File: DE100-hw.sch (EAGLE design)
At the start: 50 parts, among them IC3 74HC14D, IC4 74HC14D, U1 TLP521-4(GB), U2 TLP521-4(GB), X1 22-23-2041, X2 22-23-2031, X3 22-23-2101

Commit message: change route
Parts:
- removed H3: MOUNT-PAD-SQUARE3.0, holes:MOUNT-PAD-SQUARE3.0
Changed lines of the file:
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@@
 <part name="H1" library="holes" library_urn="urn:adsk.eagle:library:237" deviceset="MOUNT-PAD-SQUARE" device="3.0" package3d_urn="urn:adsk.eagle:package:14290/1"/>
 <part name="H2" library="holes" library_urn="urn:adsk.eagle:library:237" deviceset="MOUNT-PAD-SQUARE" device="3.0" package3d_urn="urn:adsk.eagle:package:14290/1"/>
-<part name="H3" library="holes" library_urn="urn:adsk.eagle:library:237" deviceset="MOUNT-PAD-SQUARE" device="3.0" package3d_urn="urn:adsk.eagle:package:14290/1"/>
 </parts>
 <sheets>
@@
 <attribute name="VALUE" x="165.354" y="2.6162" size="1.778" layer="96"/>
 </instance>
-<instance part="H3" gate="G$1" x="154.94" y="5.08" smashed="yes">
-<attribute name="NAME" x="157.734" y="5.6642" size="1.778" layer="95"/>
-<attribute name="VALUE" x="157.734" y="2.6162" size="1.778" layer="96"/>
-</instance>
 </instances>

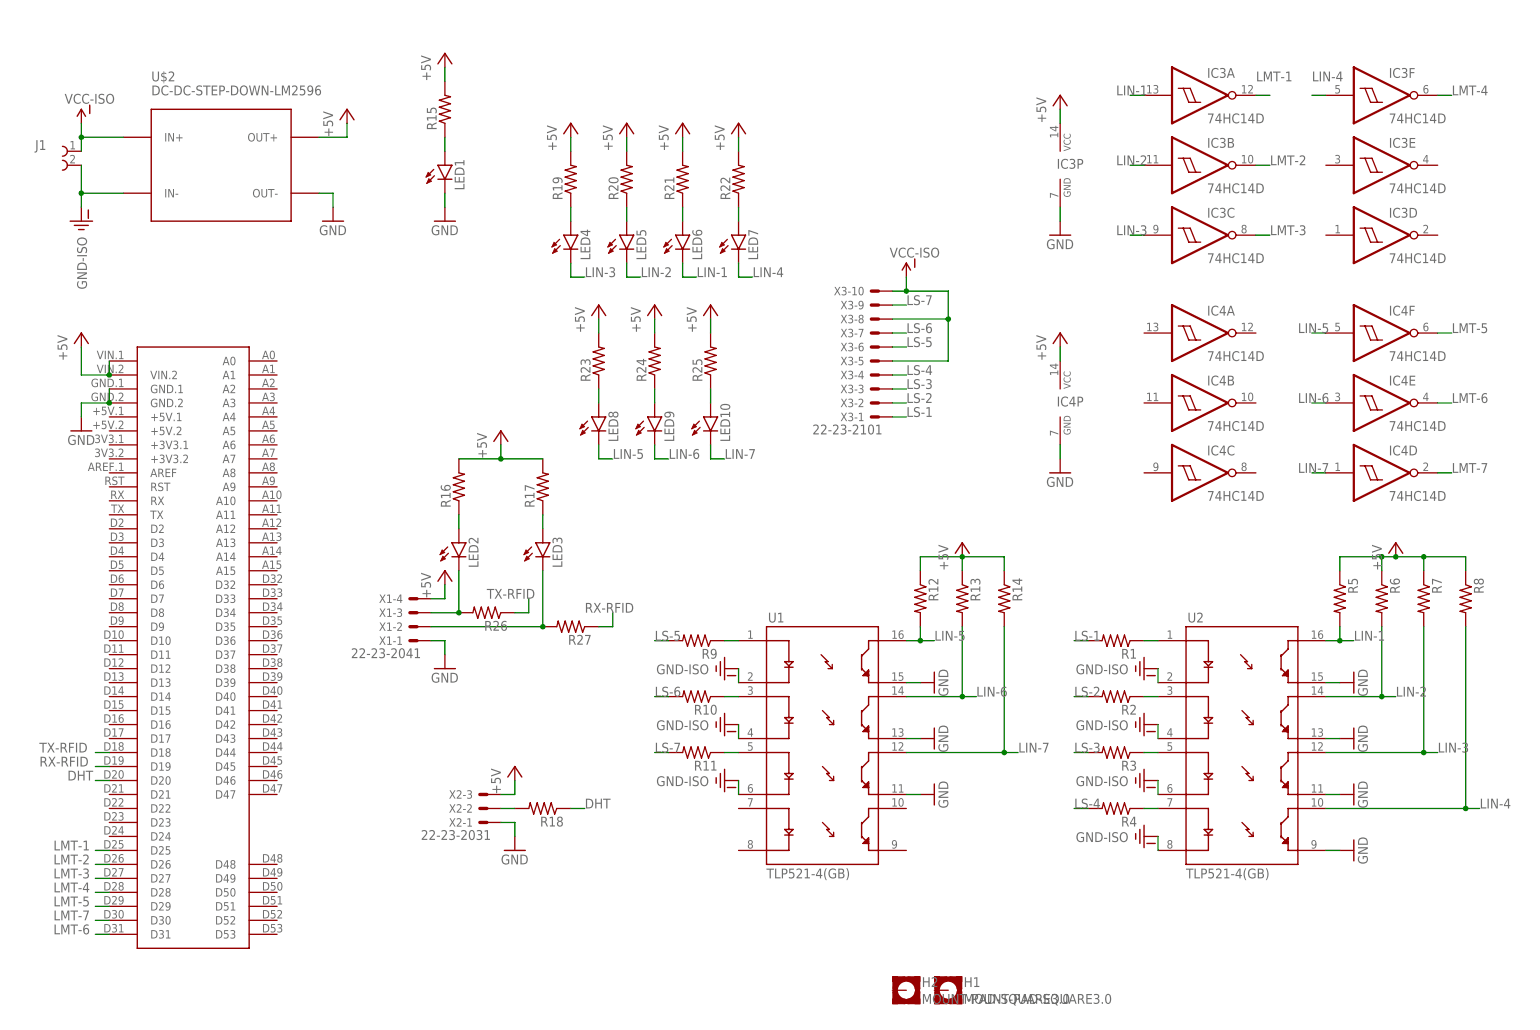
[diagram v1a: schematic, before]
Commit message: add additional name and gerber file
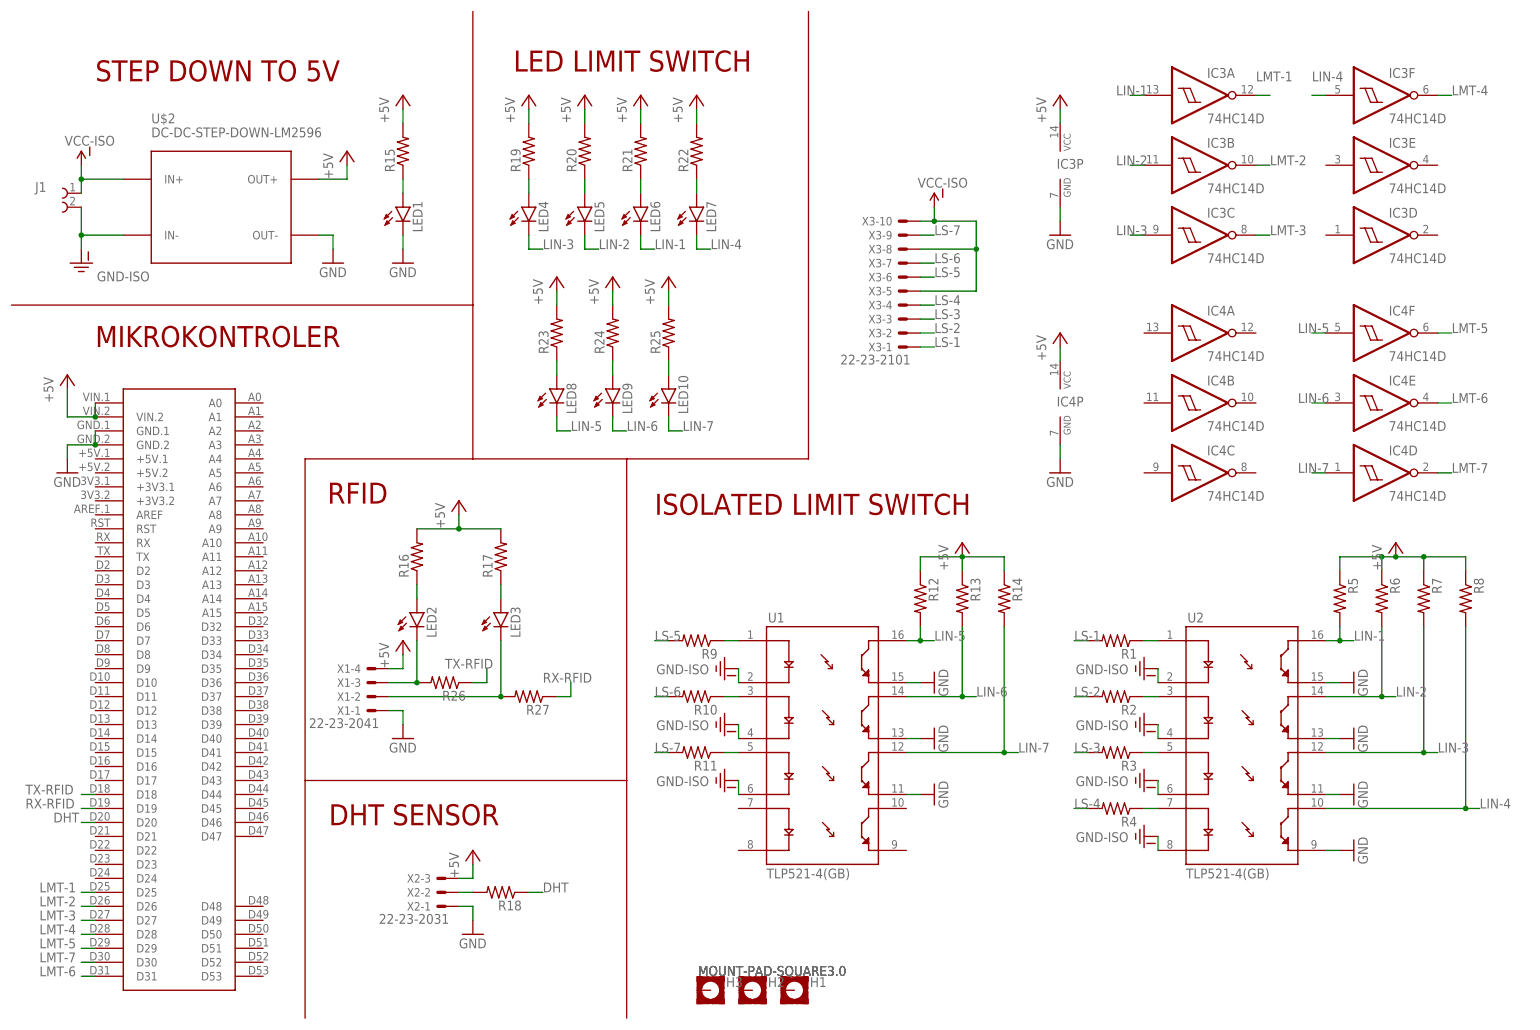
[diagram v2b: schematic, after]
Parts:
- added H3: MOUNT-PAD-SQUARE3.0, holes:MOUNT-PAD-SQUARE3.0
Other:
- note added: "DHT SENSOR"
- note added: "ISOLATED LIMIT SWITCH"
- note added: "LED LIMIT SWITCH"
- note added: "MIKROKONTROLER"
- note added: "RFID"
- note added: "STEP DOWN TO 5V"
- moved on the sheet: H1, H2, J1, LED1, LED10, LED2, LED3, LED4, LED5, LED6, LED7, LED8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

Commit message: add hole
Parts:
- added H4: MOUNT-PAD-SQUARE3.0, holes:MOUNT-PAD-SQUARE3.0
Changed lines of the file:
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@@
 <part name="H2" library="holes" library_urn="urn:adsk.eagle:library:237" deviceset="MOUNT-PAD-SQUARE" device="3.0" package3d_urn="urn:adsk.eagle:package:14290/1"/>
 <part name="H3" library="holes" library_urn="urn:adsk.eagle:library:237" deviceset="MOUNT-PAD-SQUARE" device="3.0" package3d_urn="urn:adsk.eagle:package:14290/1"/>
+<part name="H4" library="holes" library_urn="urn:adsk.eagle:library:237" deviceset="MOUNT-PAD-SQUARE" device="3.0" package3d_urn="urn:adsk.eagle:package:14290/1"/>
 </parts>
 <sheets>
@@
 <attribute name="VALUE" x="124.714" y="7.6962" size="1.778" layer="96"/>
 </instance>
+<instance part="H4" gate="G$1" x="119.38" y="5.08" smashed="yes">
+<attribute name="NAME" x="122.174" y="5.6642" size="1.778" layer="95"/>
+<attribute name="VALUE" x="124.714" y="7.6962" size="1.778" layer="96"/>
+</instance>
